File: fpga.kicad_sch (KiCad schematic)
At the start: 60 parts, among them J8 2X05, Q13 2N7002, U12 SC18IS602BIPW, U13 W25Q32JVSSIQ, Y2 OSC40M-3.3_S5

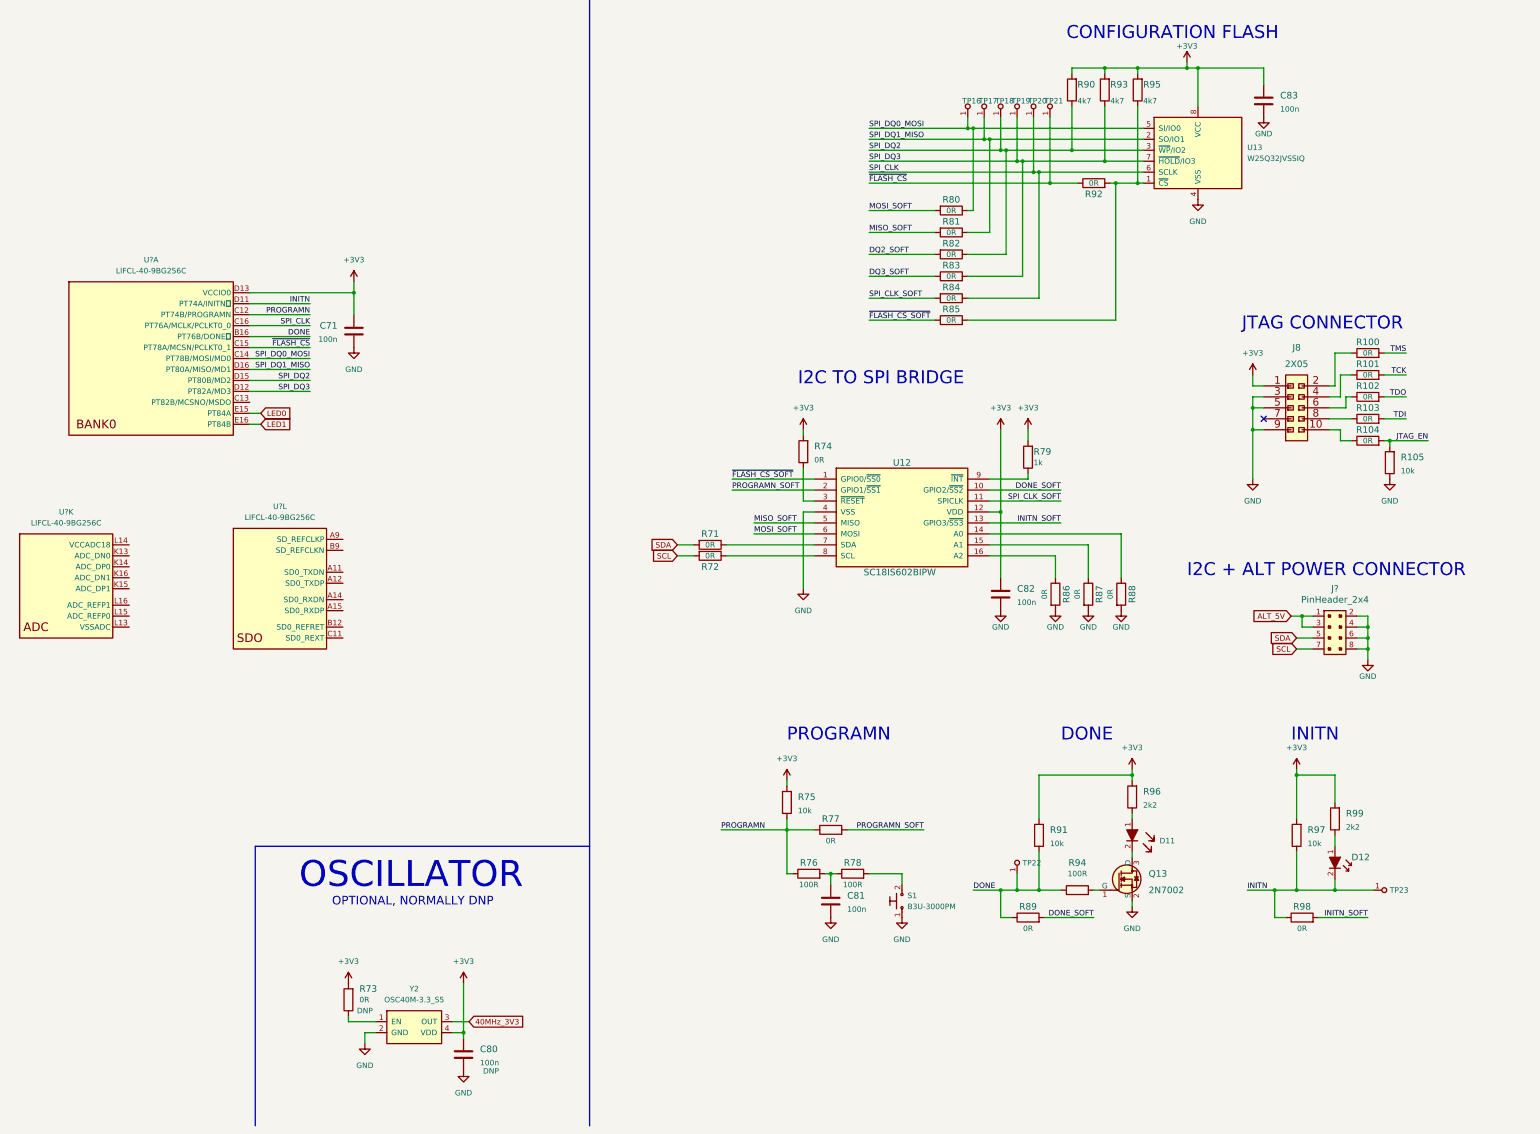
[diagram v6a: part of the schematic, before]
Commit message: Modified power indicator and connected unused pins
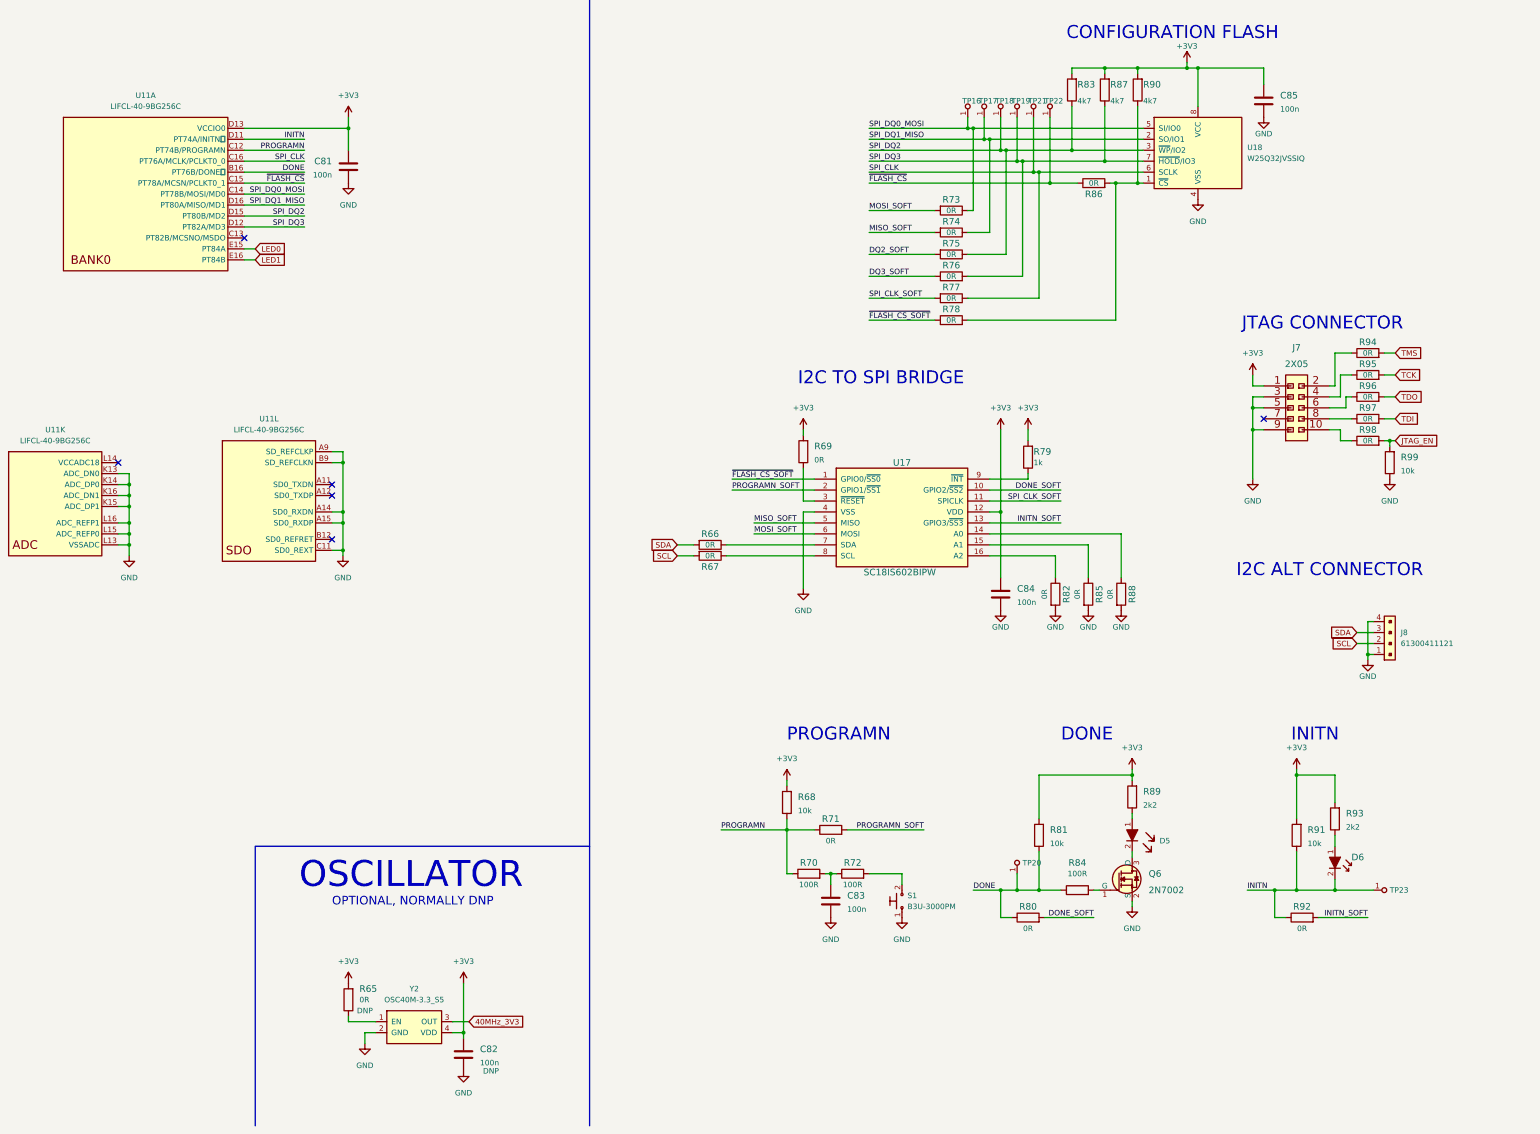
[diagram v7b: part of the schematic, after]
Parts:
- removed J?: PinHeader_2x4, antmicro-footprints:PinHeader_2x04_P2.54mm_Vertical, symbol antmicroRectangularConnectorsHeadersMalePins:PinHeader_2x4
- added J8: 61300411121, antmicro-footprints:PinHeader_1x4_P2.54mm_Drill1.02mm, symbol antmicroRectangularConnectorsHeadersMalePins:61300411121
- gave numbers to parts that had none: 1
- renumbered C71 to C81, C80 to C82, C81 to C83, C82 to C84, C83 to C85, D11 to D5, D12 to D6, J8 to J7, Q13 to Q6, R73 to R65, R71 to R66, R72 to R67, R75 to R68, R74 to R69, R76 to R70, R77 to R71, R78 to R72, R80 to R73, R81 to R74, R82 to R75, R83 to R76, R84 to R77, R85 to R78, R89 to R80, R91 to R81, R86 to R82, R90 to R83, R94 to R84, R87 to R85, R92 to R86, R93 to R87, R96 to R89, R95 to R90, R97 to R91, R98 to R92, R99 to R93, R100 to R94, R101 to R95, R102 to R96, R103 to R97, R104 to R98, R105 to R99, TP22 to TP20, TP20 to TP21, TP21 to TP22, U12 to U17, U13 to U18
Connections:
- net GND: now also U11.A14 (SD0_RXDN), U11.A15 (SD0_RXDP), U11.A9 (SD_REFCLKP), U11.B9 (SD_REFCLKN), U11.C11 (SD0_REXT), U11.K13 (ADC_DN0), U11.K14 (ADC_DP0), U11.K15 (ADC_DP1), U11.K16 (ADC_DN1), U11.L13 (VSSADC), U11.L15 (ADC_REFP0), U11.L16 (ADC_REFP1), J8.1, J8.4
- net SCL: now also J8.2
- net SDA: now also J8.3
- no-connect marks 1 -> 6
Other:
- note added: "I2C ALT CONNECTOR"
- note removed: "I2C + ALT POWER CONNECTOR"
- moved on the sheet: C81, U11A, U11K, U11L
